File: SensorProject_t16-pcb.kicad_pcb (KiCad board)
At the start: 2 copper layers, 48.3 x 71.1 mm, 60 parts, among them J1 Conn_01x02_Pin, J10 Conn_01x02_Pin, J11 Conn_01x02_Pin, J12 Conn_01x02_Pin, J13 Conn_01x02_Pin, J14 Conn_01x02_Pin, J15 Conn_01x02_Pin, J16 Conn_01x02_Pin, J17 Conn_01x04_Pin, J18 PinSocket_1x20_P2.54mm_Vertic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, J19 PinSocket_1x20_P2.54mm_Vertic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, J2 Conn_01x02_Pin, J20 Screw_Terminal_01x02, J3 Conn_01x02_Pin, J4 Conn_01x02_Pin, J5 Conn_01x02_Pin, J6 Conn_01x02_Pin, J7 Conn_01x02_Pin, J8 Conn_01x02_Pin, J9 Conn_01x02_Pin, U1 ADS1115IDGS, U2 ADS1115IDGS, U3 ADS1115IDGS, U4 ADS1115IDGS

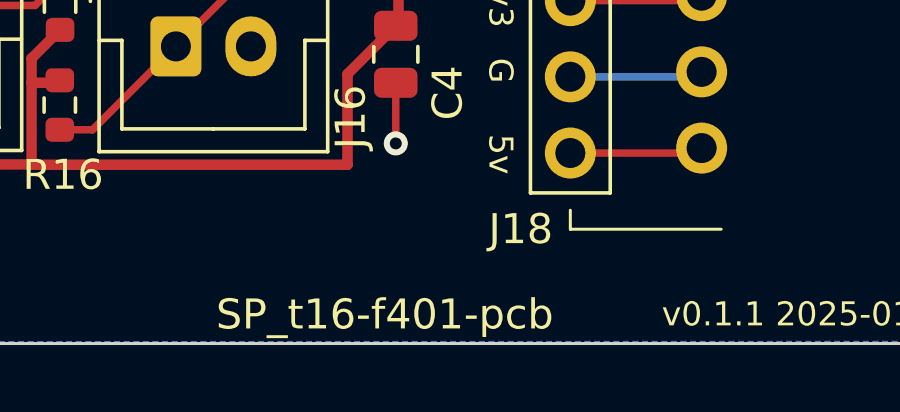
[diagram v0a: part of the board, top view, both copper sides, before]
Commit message: Adjusted rename for better convention.
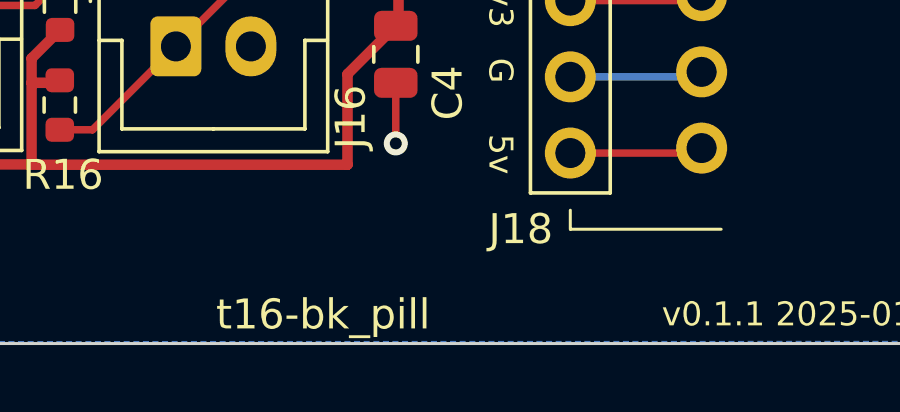
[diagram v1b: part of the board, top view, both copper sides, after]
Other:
- board text added: "t16-bk_pill"
- board text removed: "SP_t16-f401-pcb"

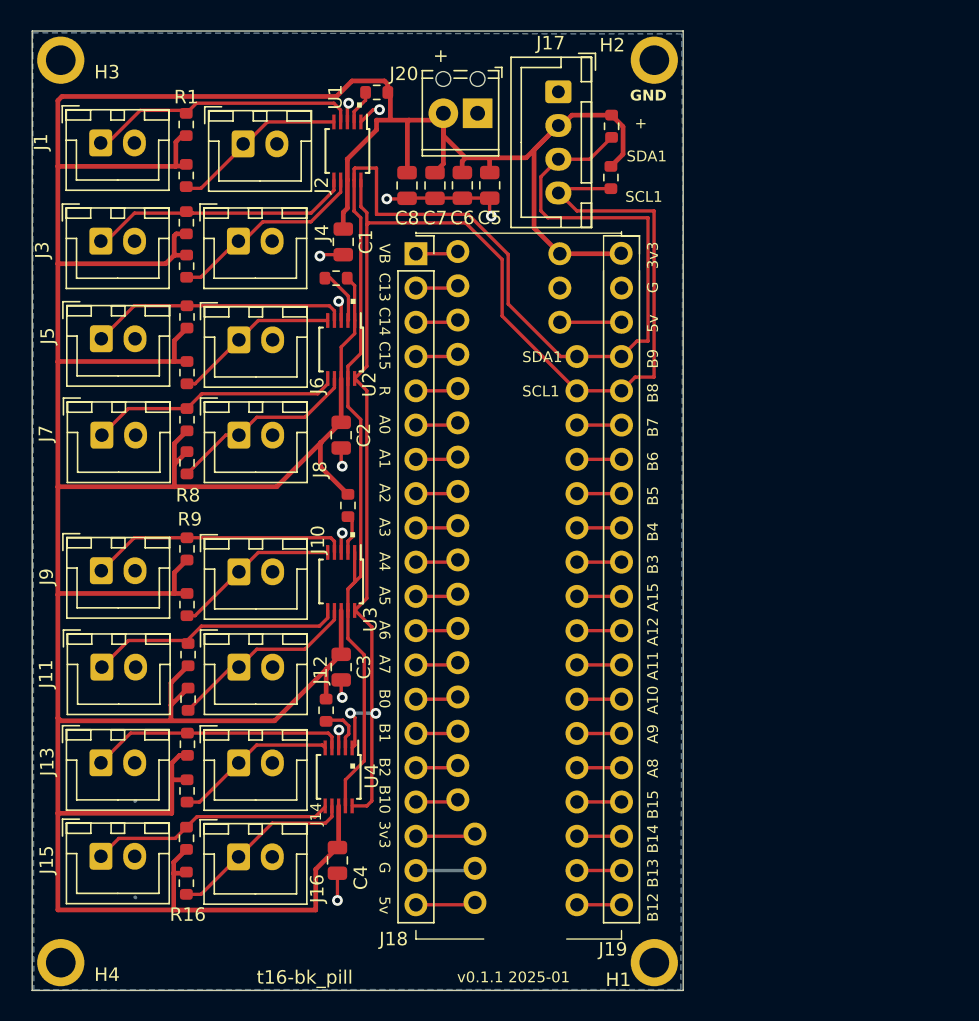
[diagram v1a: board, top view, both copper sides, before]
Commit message: layout with F411 roughly good but needs work.
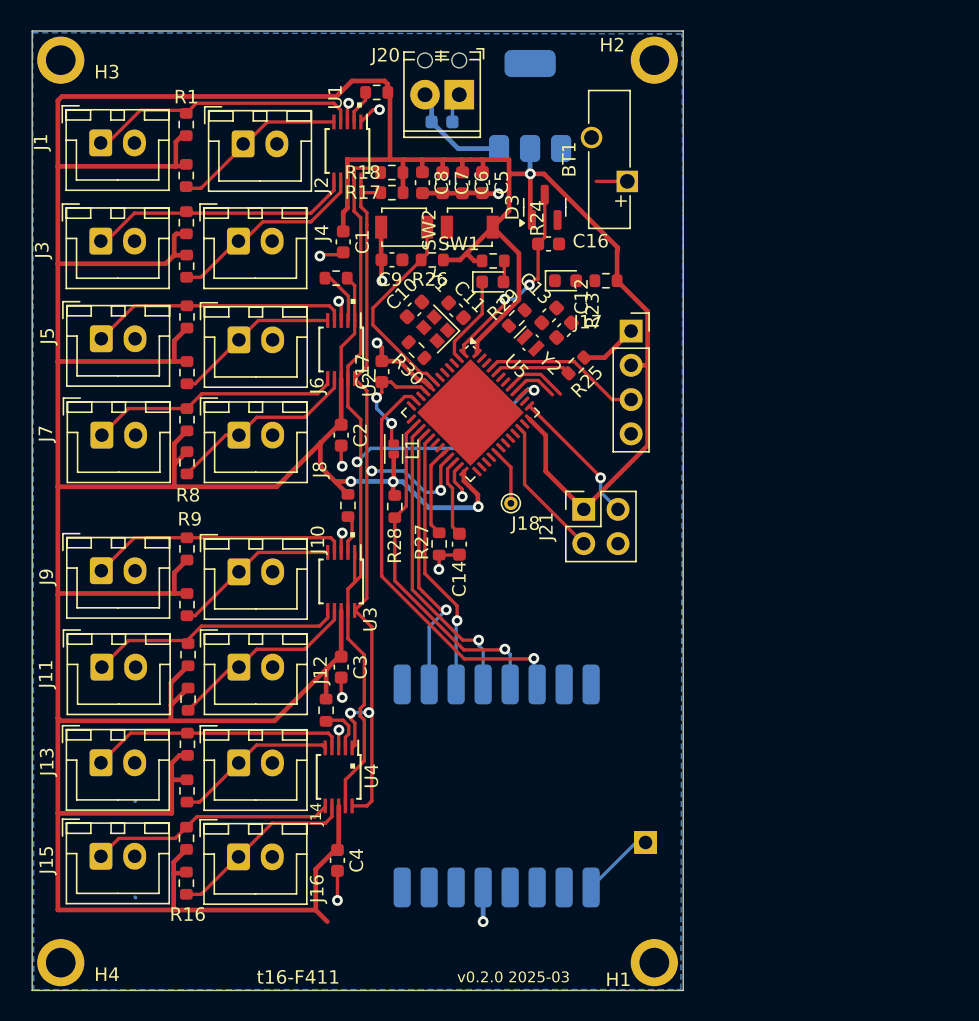
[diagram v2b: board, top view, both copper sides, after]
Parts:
- removed J**1: SolderWire-0.25sqmm_1x20_P4.2mm_D0.65mm_OD1.7mm, ProjectLib:b_pill_takeoffPads_1-20
- removed J**2: SolderWire-0.25sqmm_1x20_P4.2mm_D0.65mm_OD1.7mm, ProjectLib:b_pill_takeoffPads_21-40
- removed J19: PinSocket_1x20_P2.54mm_Vertical, ProjectLib:b_pill_socket_21-40
- added AE1: 915mhz antenna, ProjectLib:915MHz_spring_antenna, B.Cu at (95.0, 84.3)
- added BT1: Battery_Cell, ProjectLib:Battery_Panasonic_CR1025-VSK_Vertical_CircularHoles, F.Cu at (93.6, 35.3)
- added C10: 6pF C0G, NP0, +/- 0.1pF, ProjectLib:C_0603_1608Metric, F.Cu at (77.9, 44.8)
- added C11: 6pF C0G, NP0, +/- 0.1pF, ProjectLib:C_0603_1608Metric, F.Cu at (81.0, 44.8)
- added C12: 4pF C0G, NP0, +/- 0.1pF, ProjectLib:C_0603_1608Metric, F.Cu at (89.0, 46.3)
- added C13: 4pF C0G, NP0, +/- 0.1pF, ProjectLib:C_0603_1608Metric, F.Cu at (87.9, 45.2)
- added C14: 4.7uF, ProjectLib:C_0603_1608Metric, F.Cu at (81.2, 62.2)
- added C15: 100nF, ProjectLib:C_0603_1608Metric, B.Cu at (79.9, 30.9)
- added C16: 100nF, ProjectLib:C_0603_1608Metric, F.Cu at (87.8, 39.9)
- added C17: 100n, ProjectLib:C_0603_1608Metric, F.Cu at (75.5, 49.4)
- added C9: 100nF, ProjectLib:C_0603_1608Metric, F.Cu at (76.2, 41.1)
- added D1: red, ProjectLib:LED_0603_1608Metric, F.Cu at (89.1, 42.6)
- added D2: blue, ProjectLib:LED_0603_1608Metric, F.Cu at (83.7, 42.7)
- added D3: BAT54C, ProjectLib:SOT-23, F.Cu at (87.5, 37.2)
- added J21: Conn_01x04_Pin, ProjectLib:PinSocket_2x02_P2.54mm_Vertical, F.Cu at (90.4, 59.6)
- added L1: 2.2uH, ProjectLib:L_TDK_MLZ1608, F.Cu at (76.3, 55.1)
- added R23: 0K4, ProjectLib:R_0603_1608Metric, F.Cu at (92.1, 42.6)
- added R24: 0K1, ProjectLib:R_0603_1608Metric, F.Cu at (83.7, 41.2)
- added R25: 10k 1%, ProjectLib:R_0603_1608Metric, F.Cu at (89.9, 48.9)
- added R26: 10k 1%, ProjectLib:R_0603_1608Metric, F.Cu at (79.2, 41.1)
- added R27: 10k 1%, ProjectLib:R_0603_1608Metric, F.Cu at (79.7, 62.1)
- added R28: 10k 1%, ProjectLib:R_0603_1608Metric, F.Cu at (76.4, 59.4)
- added R29: CHECK K 1%, ProjectLib:R_0603_1608Metric, F.Cu at (85.5, 45.4)
- added R30: 1.1k 1%, ProjectLib:R_0603_1608Metric, F.Cu at (78.0, 47.8)
- added SW1: SW_Push, ProjectLib:SW_SPST_B3U-1000P, F.Cu at (77.1, 38.7)
- added SW2: SW_Push, ProjectLib:SW_SPST_B3U-1000P, F.Cu at (82.0, 38.7)
- added U5: STM32F411CEUx, ProjectLib:QFN-48-1EP_7x7mm_P0.5mm_EP5.6x5.6mm, F.Cu at (82.0, 52.4)
- added U6: AMS1117-3.3, ProjectLib:SOT-223, B.Cu at (86.4, 29.7)
- added U7: RFM95W-915S2, ProjectLib:HOPERF_RFM9XW_SMD, B.Cu at (84.0, 80.1)
- added Y1: 25MHz, ProjectLib:Crystal_SMD_2016-4Pin_2.0x1.6mm, F.Cu at (79.4, 46.2)
- added Y2: 32.758kHz, ProjectLib:Crystal_SMD_MicroCrystal_CM9V-T1A-2Pin_1.6x1.0mm, F.Cu at (86.5, 47.2)
- C1, C2, C3, C4: footprint ProjectLib:C_0805_2012Metric -> ProjectLib:C_0603_1608Metric
- C5: value 10µF -> 1µF; footprint ProjectLib:C_0805_2012Metric -> ProjectLib:C_0603_1608Metric
- C6, C7, C8: value 10µF -> 100nF; footprint ProjectLib:C_0805_2012Metric -> ProjectLib:C_0603_1608Metric
- J17: value Conn_01x04_Pin -> Conn_01x04_Socket; footprint ProjectLib:JST_XH_B4B-XH-A_1x04_P2.50mm_Vertical -> ProjectLib:PinSocket_1x04_P2.54mm_Vertical
- J18: value PinSocket_1x20_P2.54mm_Vertical -> THTPad; footprint ProjectLib:b_pill_socket_1-20 -> ProjectLib:TestPoint_THTPad_D1.0mm_Drill0.5mm
- R1, R10, R11, R12, R13, R14, R15, R16, R17, R18, R19, R2, R20, R21, R22, R3, R4, R5, R6, R7, R8, R9: value 10k -> 10k 1%
- moved J17 18.5 mm to (93.9, 46.4), turned to 0 degrees
- moved R18 16.6 mm to (76.2, 34.6), turned to 180 degrees
- moved R17 16.3 mm to (76.2, 36.1), turned to 180 degrees
- moved J18 9.02 mm to (85.0, 59.1)
- moved J20 1.93 mm to (81.2, 28.9)
- moved C8 1.16 mm to (78.5, 35.4)
- moved C7 0.61 mm to (80.0, 35.4)
- moved C5 0.58 mm to (82.9, 35.4)
- moved C6 0.19 mm to (81.4, 35.4)
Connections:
- J17 pad 3: /SDA1 -> SCL2
- J17 pad 4: /SCL1 -> SDA2
- J20 pad 2: +3V3 -> +5V
- R17 pad 2: /SCL1 -> SCL1
- R18 pad 2: /SDA1 -> SDA1
- U1 pad 10: /SCL1 -> SCL1
- U1 pad 9: /SDA1 -> SDA1
- U2 pad 10: /SCL1 -> SCL1
- U2 pad 9: /SDA1 -> SDA1
- U3 pad 1: /SDA1 -> SDA1
- U3 pad 10: /SCL1 -> SCL1
- U3 pad 9: /SDA1 -> SDA1
- U4 pad 1: /SCL1 -> SCL1
- U4 pad 10: /SCL1 -> SCL1
- U4 pad 9: /SDA1 -> SDA1
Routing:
- net /SDA1: track 109.7 -> 0.00 mm
- net /SCL1: track 106.6 -> 0.00 mm, vias 2 -> 0
- net SDA1: track 0.00 -> 71.7 mm, vias 0 -> 2
- net SCL1: track 0.00 -> 63.9 mm, vias 0 -> 4
- net +3V3: track 325.3 -> 384.3 mm, vias 0 -> 5
- net RESET: track 0.00 -> 30.9 mm, vias 0 -> 1
- net NSS: track 0.00 -> 25.4 mm, vias 0 -> 1
- net SCK: track 0.00 -> 22.1 mm, vias 0 -> 1
- net MISO: track 0.00 -> 20.4 mm, vias 0 -> 1
- net MOSI: track 0.00 -> 19.5 mm, vias 0 -> 1
- net Net-(U5-NRST): track 0.00 -> 15.3 mm
- net GND: track 27.5 -> 42.4 mm, vias 11 -> 14
- net VBAT: track 0.00 -> 14.8 mm, vias 0 -> 2
- net SCL2: track 0.00 -> 11.7 mm
- net /f411/SWDIO: track 0.00 -> 10.5 mm
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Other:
- board text added: "t16-F411"
- board text added: "v0.2.0 2025-03"
- board text removed: "GND"
- board text removed: "SCL1"
- board text removed: "SDA1"
- board text removed: "t16-bk_pill"
- board text removed: "v0.1.1 2025-01"

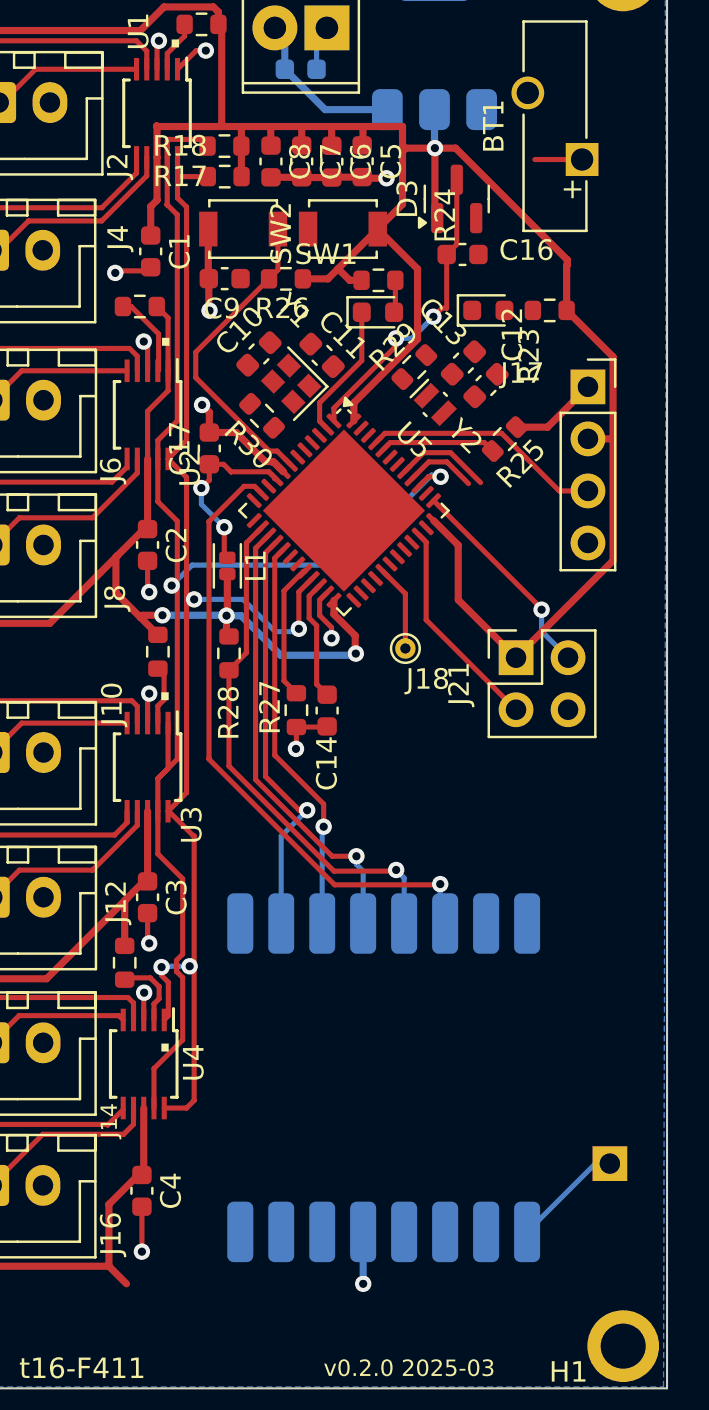
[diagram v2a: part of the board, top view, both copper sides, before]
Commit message: Most routing done but not checked. Moat around HSE but no net-tie yet.
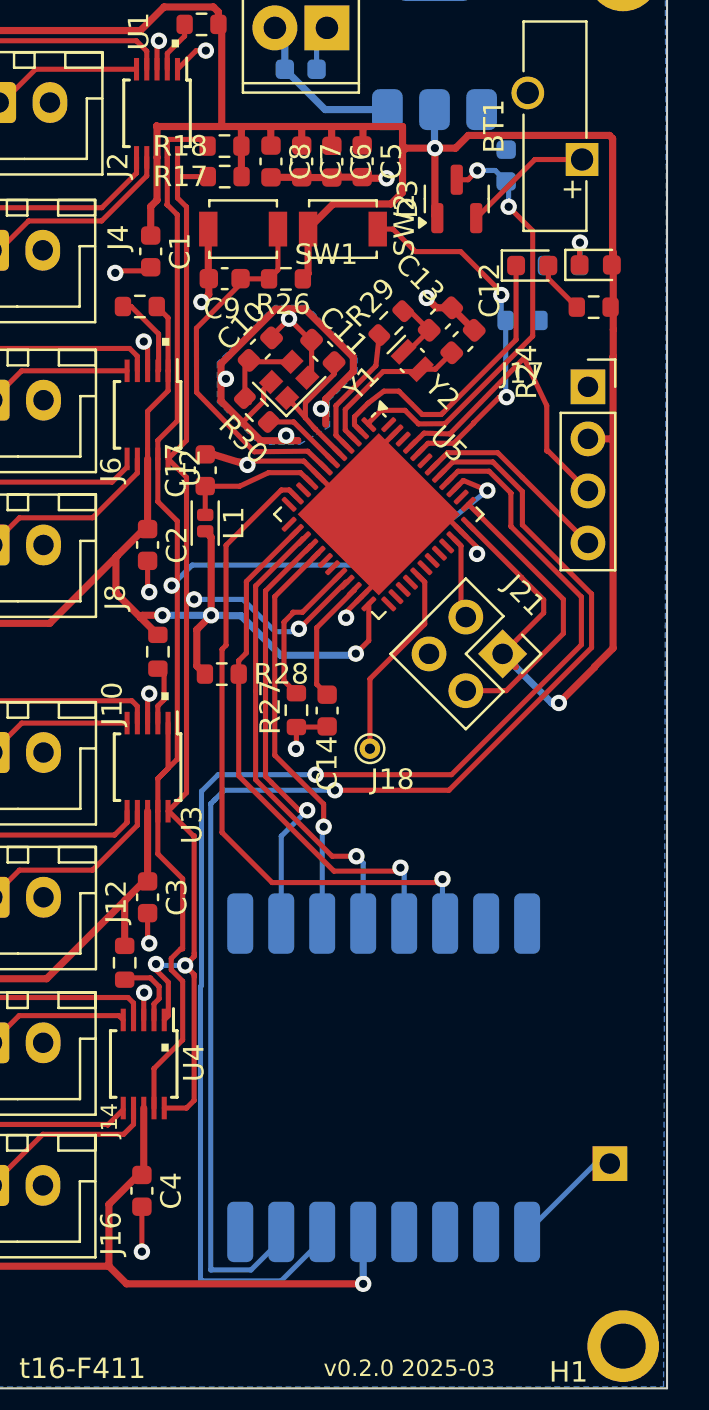
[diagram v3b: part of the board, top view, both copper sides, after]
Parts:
- C16, R23, R25: moved to B.Cu
- moved R24 10.6 mm to (94.2, 42.5), turned to 180 degrees
- moved D2 7.87 mm to (91.2, 40.5)
- moved R25 5.85 mm to (90.7, 43.1), turned to 0 degrees
- moved D1 5.69 mm to (94.3, 40.4)
- moved J18 5.19 mm to (83.3, 64.0)
- moved C16 4.83 mm to (89.9, 35.6), turned to 90 degrees
- moved R29 2.42 mm to (84.3, 43.3)
- moved Y2 2.42 mm to (85.4, 45.1)
- moved C12 2.42 mm to (87.8, 44.2)
- moved C13 2.42 mm to (86.7, 43.1)
- moved L1 2.35 mm to (75.2, 53.0)
- moved R23 2.28 mm to (92.7, 40.5)
- moved U5 1.71 mm to (83.7, 52.6)
- moved C17 1.08 mm to (75.2, 50.4)
- moved R28 1.07 mm to (76.1, 60.4), turned to 0 degrees
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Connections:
- C10 pad 1: GND -> GND_HSE
- C11 pad 1: GND -> GND_HSE
- D1 pad 1: GND -> Net-(D1-K)
- D1 pad 2: Net-(D1-A) -> +3V3
- R23 pad 1: +3V3 -> Net-(D1-K)
- R23 pad 2: Net-(D1-A) -> GND
- Y1 pad 2: GND -> Net-(Y1-Pad2)
- Y1 pad 4: GND -> Net-(Y1-Pad2)
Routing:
- net DIO0: track 3.55 -> 65.2 mm, vias 0 -> 1
- net DIO1: track 4.70 -> 62.9 mm, vias 0 -> 1
- net GND_HSE: track 0.00 -> 26.7 mm, vias 0 -> 4
- net GND: track 42.4 -> 61.5 mm, vias 14 -> 16
- net +3V3: track 384.3 -> 400.7 mm, vias 5 -> 6
- net Net-(U5-BOOT0): track 5.69 -> 18.2 mm, vias 0 -> 2
- net SDA2: track 0.00 -> 9.74 mm
- net Net-(D2-K): track 6.65 -> 14.8 mm
- net PC14_OSC32_IN: track 0.00 -> 7.98 mm
- net PH0_OSC_IN: track 0.00 -> 7.03 mm
- net PC15_OSC32_OUT: track 0.00 -> 6.47 mm
- net VBAT: track 14.8 -> 21.3 mm
- net /f411/SWDIO: track 10.5 -> 4.07 mm
- net Net-(J18-Pin_1): track 4.22 -> 9.73 mm
- net Net-(C10-Pad2): track 0.00 -> 4.15 mm
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- added copper zone on B.Cu, net GND_HSE

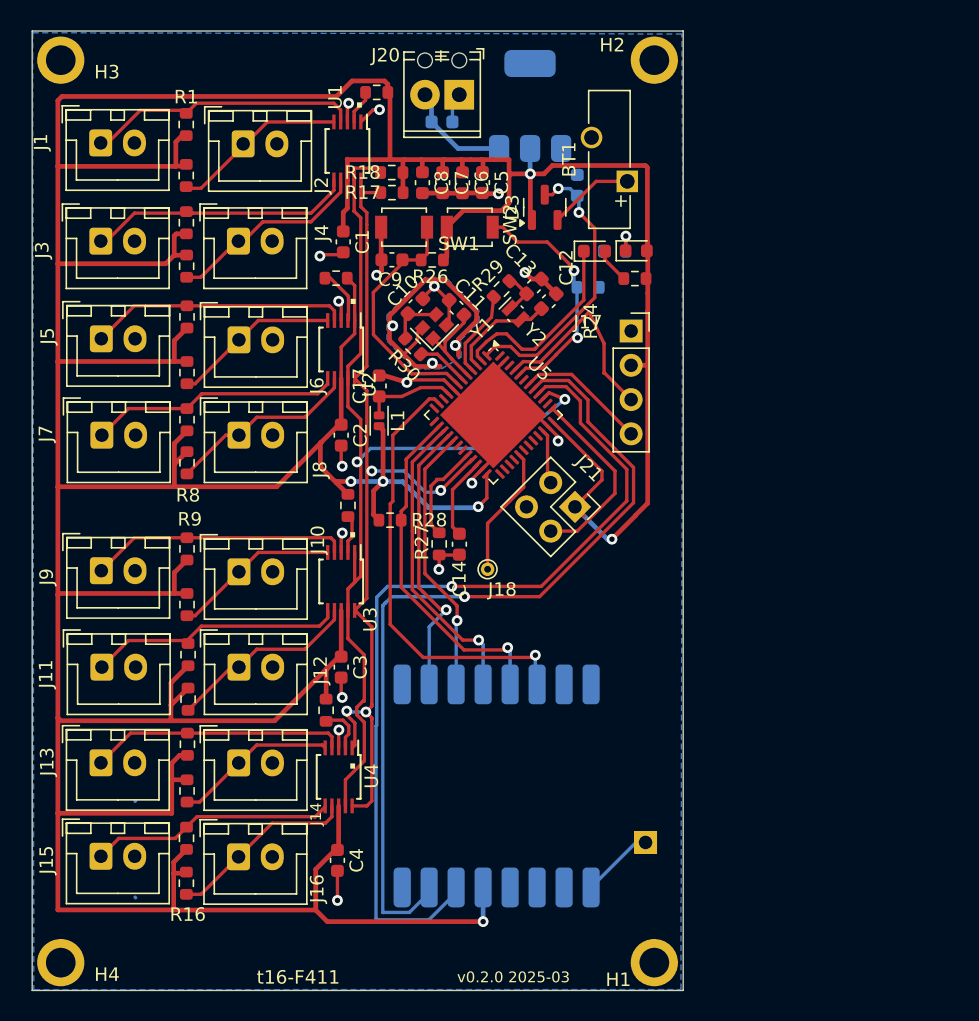
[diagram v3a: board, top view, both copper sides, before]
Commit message: Moats complete. No errors. Net tie needs better zone and check crystals, BoM, etc. And general review.
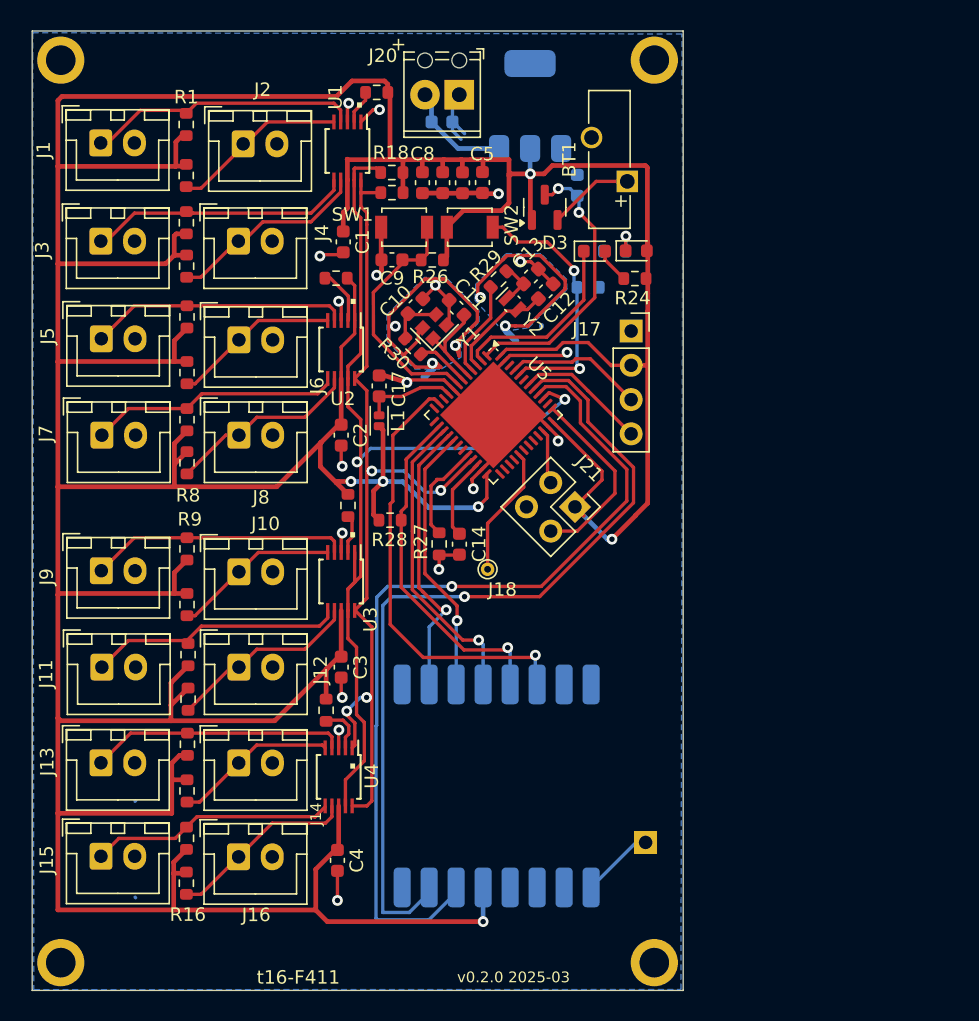
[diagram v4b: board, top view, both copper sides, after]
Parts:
- added NT1: NetTie_2, ProjectLib:NetTie-2_SMD_Pad0.5mm, B.Cu at (78.9, 49.5)
- added NT2: NetTie_2, ProjectLib:NetTie-2_SMD_Pad0.5mm, B.Cu at (85.0, 46.7)
- moved C12 0.77 mm to (87.6, 43.4)
- moved C13 0.77 mm to (86.5, 42.3)
- moved R29 0.77 mm to (84.1, 42.5)
- moved Y2 0.77 mm to (85.1, 44.4)
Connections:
- C12 pad 1: GND -> /f411/LSE/GND_LSE
- C13 pad 1: GND -> /f411/LSE/GND_LSE
- Y1 pad 2: Net-(Y1-Pad2) -> GND_HSE
- Y1 pad 4: Net-(Y1-Pad2) -> GND_HSE
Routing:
- net /f411/LSE/GND_LSE: track 0.00 -> 19.6 mm, vias 0 -> 3
- net +3V3: track 400.7 -> 411.6 mm
- net GND: track 61.5 -> 66.7 mm
- net SCL2: track 15.0 -> 10.3 mm
- net GND_HSE: track 26.7 -> 30.1 mm
- net Net-(U5-BOOT0): track 18.2 -> 19.8 mm
- net Net-(D2-K): track 14.8 -> 13.9 mm
- net PC15_OSC32_OUT: track 6.47 -> 7.17 mm
- net VBAT: track 21.3 -> 20.8 mm
- net Net-(C13-Pad2): track 3.34 -> 2.80 mm
- net SDA1: track 74.3 -> 73.8 mm
- added copper zone on B.Cu, net /f411/LSE/GND_LSE

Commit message: battery needs work.
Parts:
- BT1: footprint ProjectLib:Battery_Panasonic_CR1025-VSK_Vertical_CircularHoles -> ProjectLib:BatteryHolder_LINX_BAT-HLD-012-SMT
- J21: value Conn_01x04_Pin -> Conn_2x02_Pin
- moved BT1 15.4 mm to (108.9, 32.8), turned to 180 degrees
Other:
- board text added: "3v"
- board text added: "3v3"
- board text added: "GND"
- board text added: "SDA2"
- board text added: "SLC2"
- board text added: "SWCLK"
- board text added: "SWDI0"
- board text added: "v0.2.0 2025-04"
- board text removed: "v0.2.0 2025-03"
